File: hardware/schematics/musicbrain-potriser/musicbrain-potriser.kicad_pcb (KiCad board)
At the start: 2 copper layers, 28 x 80 mm, 12 parts, among them J1 BUS, J2 NAAR FRONT, U1 MCP3208

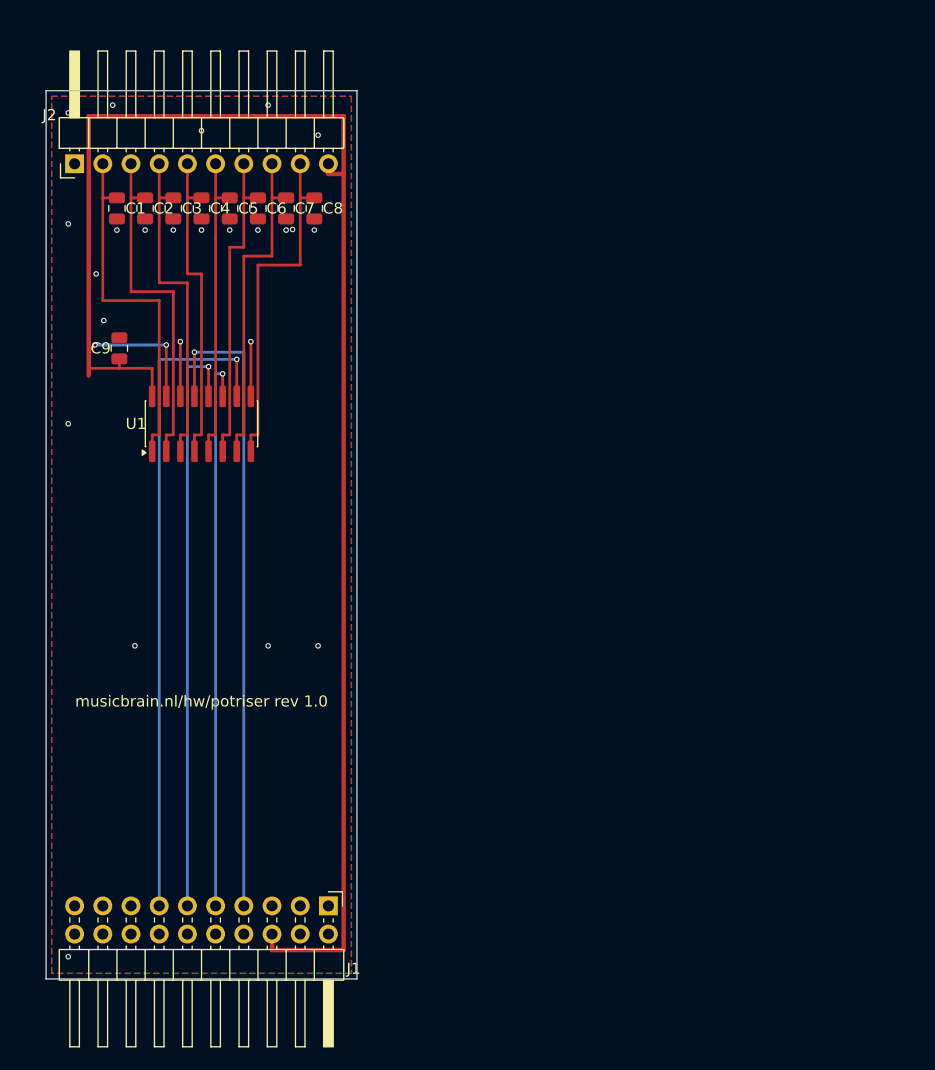
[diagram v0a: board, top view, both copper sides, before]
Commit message: Gen 2 stap 3b/3c: riser + potriser rev 2.0 (2x12, H=50) DRC 0/0
riser: 40x50, hele 2x12-bus 1-op-1 omhoog incl. de audio-lijnen ->
ontwikkelbord voor een gedelegeerde Teensy/FPGA. x-matching schaalt mee:
J2-pin q draagt slotfunctie (24-q) oneven / (26-q) even.

potriser: 28x80 -> 80x50, J1 2x12; koper via freerouting i.p.v. handlanen
(1 unrouted -> snap_stubs dichtte 'm). Front-contract 1x10 ongewijzigd.

Meetvondst: de connector-bodies hangen bewust OVER de bordrand (zo mateert
de kaart met de socket eronder) -- dus de vrije kernband bij H=50 is 33,3 mm,
niet 18,8 zoals ik eerst schatte. Daarmee komt elke kaart op 80x50 uit op
5-16% dichtheid (adc8, de drukste: 15,6%) -- lager dan de huidige ~17% op
80 mm hoog. H=50 is dus ruim haalbaar voor alle kaarten.

Alle drie de risers: ERC 0 / netcheck OK / DRC 0/0.

Co-Authored-By: Claude Fable 5 <noreply@anthropic.com>
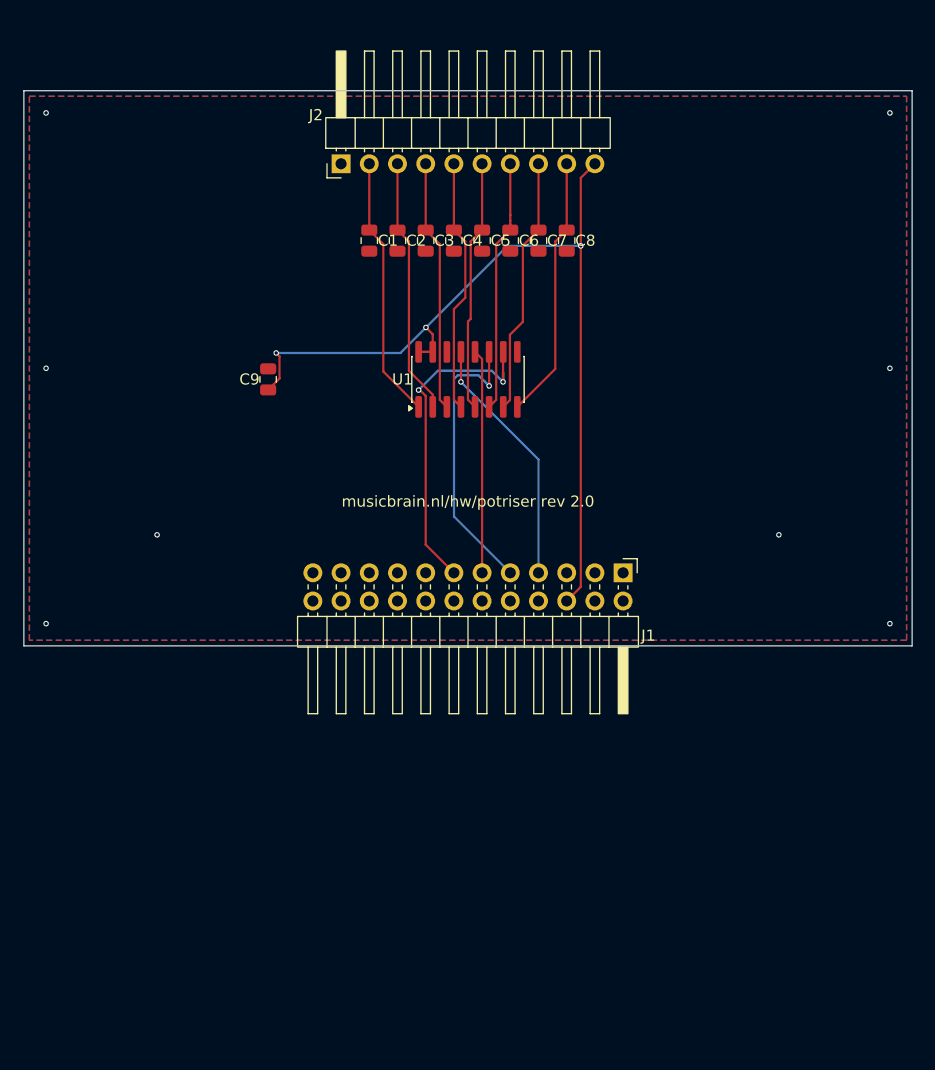
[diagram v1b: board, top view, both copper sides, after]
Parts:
- J1: footprint Connector_PinHeader_2.54mm:PinHeader_2x10_P2.54mm_Horizontal -> Connector_PinHeader_2.54mm:PinHeader_2x12_P2.54mm_Horizontal
- moved J1 40.1 mm to (154.0, 143.4)
- moved U1 24.3 mm to (140.0, 126.0)
- moved J2 24.0 mm to (128.6, 106.6)
- moved C1 22.9 mm to (131.1, 113.5)
- moved C2 22.9 mm to (133.7, 113.5)
- moved C3 22.9 mm to (136.2, 113.5)
- moved C5 22.9 mm to (141.3, 113.5)
- moved C6 22.9 mm to (143.8, 113.5)
- moved C4 22.9 mm to (138.7, 113.5)
- moved C7 22.9 mm to (146.3, 113.5)
- moved C8 22.9 mm to (148.9, 113.5)
- moved C9 13.7 mm to (122.0, 126.0)
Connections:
- J1 pad 20: (no net) -> GND
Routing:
- net +3V3: track 152.5 -> 80.7 mm, vias 2 -> 3
- net /SCLK: track 58.3 -> 22.8 mm
- net /MISO: track 53.2 -> 20.2 mm, vias 1 -> 0
- net /CS: track 59.5 -> 32.7 mm, vias 1 -> 2
- net /MOSI: track 50.6 -> 26.3 mm
- net GND: track 9.85 -> 0.00 mm, vias 24 -> 8
- net /W1: track 32.9 -> 23.7 mm
- net /W2: track 31.6 -> 23.2 mm
- net /W8: track 31.6 -> 23.7 mm
- net /W3: track 30.3 -> 22.7 mm
- net /W7: track 30.3 -> 23.2 mm
- net /W6: track 29.1 -> 22.7 mm
- net /W4: track 29.1 -> 23.0 mm
- net /W5: track 27.8 -> 22.7 mm
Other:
- board size 28 x 80 mm -> 80 x 50 mm
- board text added: "musicbrain.nl/hw/potriser rev 2.0"
- board text removed: "musicbrain.nl/hw/potriser rev 1.0"

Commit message: Release-archief rel-v0.2 per bord + paneel-inzet-fix (vondst Mark)
rel-v0.2/: de laatste gen-1-stand (2x10, H=80) van elk bord als bevroren
map naast de levende bestanden — KiCad-bronnen, README, overzicht, widget,
pinouts, bom/cpl. Gerbers zijn regenereerbaar (12574b3). Git-tag
hw-rel-v0.2 op f9eb436 markeert dezelfde stand repo-breed; prefix-tags
(hw-/fw-/web-) zijn de monorepo-conventie voor deelreleases.

Inzet-fix: de 1-rijer paneel-header gebruikte de 2-rijer-inzet (6,58),
waardoor de body 2,54 vóór de rand eindigde en de pin maar 3,46 mm in de
front-socket greep (i.p.v. 6,0). Nu per type: bus 6,58 / paneel 4,04 —
body eindigt exact op de rand, volle pin steekt uit. Beide risers
geregenereerd + potriser gerouteerd: DRC 0/0.

Co-Authored-By: Claude Fable 5 <noreply@anthropic.com>
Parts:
- moved J2 2.54 mm to (128.6, 104.0)
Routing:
- net +3V3: track 80.7 -> 94.4 mm, vias 3 -> 0
- net /W3: track 22.7 -> 33.7 mm, vias 0 -> 1
- net /CS: track 32.7 -> 24.7 mm, vias 2 -> 1
- net /SCLK: track 22.8 -> 30.6 mm, vias 1 -> 2
- net /MOSI: track 26.3 -> 22.1 mm, vias 1 -> 2
- net /W2: track 23.2 -> 26.3 mm
- net /W7: track 23.2 -> 26.0 mm
- net /W5: track 22.7 -> 25.5 mm
- net /W6: track 22.7 -> 25.3 mm
- net /W4: track 23.0 -> 25.6 mm
- net /W8: track 23.7 -> 26.3 mm
- net /W1: track 23.7 -> 26.3 mm

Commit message: gen 2: kaarthoogte 50 -> 45 mm; potriser-herroute (U1 rot 270)
- bus.py: H=45 (band 30,84 mm = bewezen gen-1-dichtheid)
- gen_riser/gen_i2criser/gen_potriser: y-literals geparametriseerd op
  bus.BY0/BY1; potriser leest nu ook gnd_stitch.json in
- potriser: U1 rot 90 -> 270 (kanalen noord, SPI+GND zuid) - bij rot 90
  wikkelden de wiper-banen zich om pad 14 (AGND) en raakte die los van
  het vlak; nieuwe freerouting (0 unrouted) + 1 hechtvia
- alle drie risers: ERC 0, netcheck OK, DRC 0/0 op 40x45 (potriser 80x45)
- docs: spi-bus-spec + systeem-v3-plan H=50 -> H=45, jack4-kabelnotitie

Co-Authored-By: Claude Fable 5 <noreply@anthropic.com>
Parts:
- moved J1 5.00 mm to (154.0, 138.4)
- turned U1 to 270 degrees
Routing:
- net +3V3: track 94.4 -> 65.7 mm
- net /SCLK: track 30.6 -> 12.3 mm, vias 2 -> 0
- net /CS: track 24.7 -> 10.7 mm, vias 1 -> 0
- net /MISO: track 20.2 -> 10.7 mm
- net /W8: track 26.3 -> 34.0 mm, vias 0 -> 1
- net /W1: track 26.3 -> 33.9 mm
- net /MOSI: track 22.1 -> 15.3 mm, vias 2 -> 0
- net /W4: track 25.6 -> 20.3 mm
- net /W7: track 26.0 -> 30.1 mm
- net /W2: track 26.3 -> 29.8 mm
- net /W3: track 33.7 -> 35.5 mm
- net /W6: track 25.3 -> 26.7 mm, vias 0 -> 2
- net GND: vias 8 -> 9
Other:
- board size 80 x 50 mm -> 80 x 45 mm

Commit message: afslank-ronde: potriser 40, gatein8 50, gate8 55, dac8 60, adc8 65 (x45)
80 mm was een maximum, geen eis (observatie Mark): J1/J2 blijven op de
hartlijn, de rand schuift naar binnen. Silk verticaal in de westrand
(horizontaal paste niet meer); hoekvia's geparametriseerd op BX0/BX1;
zwervers mee (gate8 C1, dac8 C3, adc8 JP1). Alle vijf opnieuw geroute
(verse SES) en op ERC 0 + netcheck OK + DRC 0/0.

Co-Authored-By: Claude Fable 5 <noreply@anthropic.com>
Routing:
- net /W4: track 20.3 -> 33.7 mm
- net /W5: track 25.1 -> 20.3 mm
- net /W3: track 35.5 -> 39.9 mm, vias 1 -> 0
- net /W2: track 29.8 -> 31.3 mm
- net /W8: track 34.0 -> 33.2 mm, vias 1 -> 0
- net +3V3: track 65.7 -> 65.0 mm
- net /W6: track 26.7 -> 26.5 mm, vias 2 -> 0
- net GND: vias 9 -> 12
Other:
- board size 80 x 45 mm -> 40 x 45 mm
